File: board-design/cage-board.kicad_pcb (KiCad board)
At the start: 2 copper layers, 127 x 127 mm, 48 parts, among them J1 Jack-DC, J10 73131-0240, J11 73131-0240, J12 73131-0240, J13 Conn_01x02, J14 Conn_01x02, J2 Conn_02x17_Ribbon, J3 TB002-500-03BE, J4 73131-0240, J5 73131-0240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

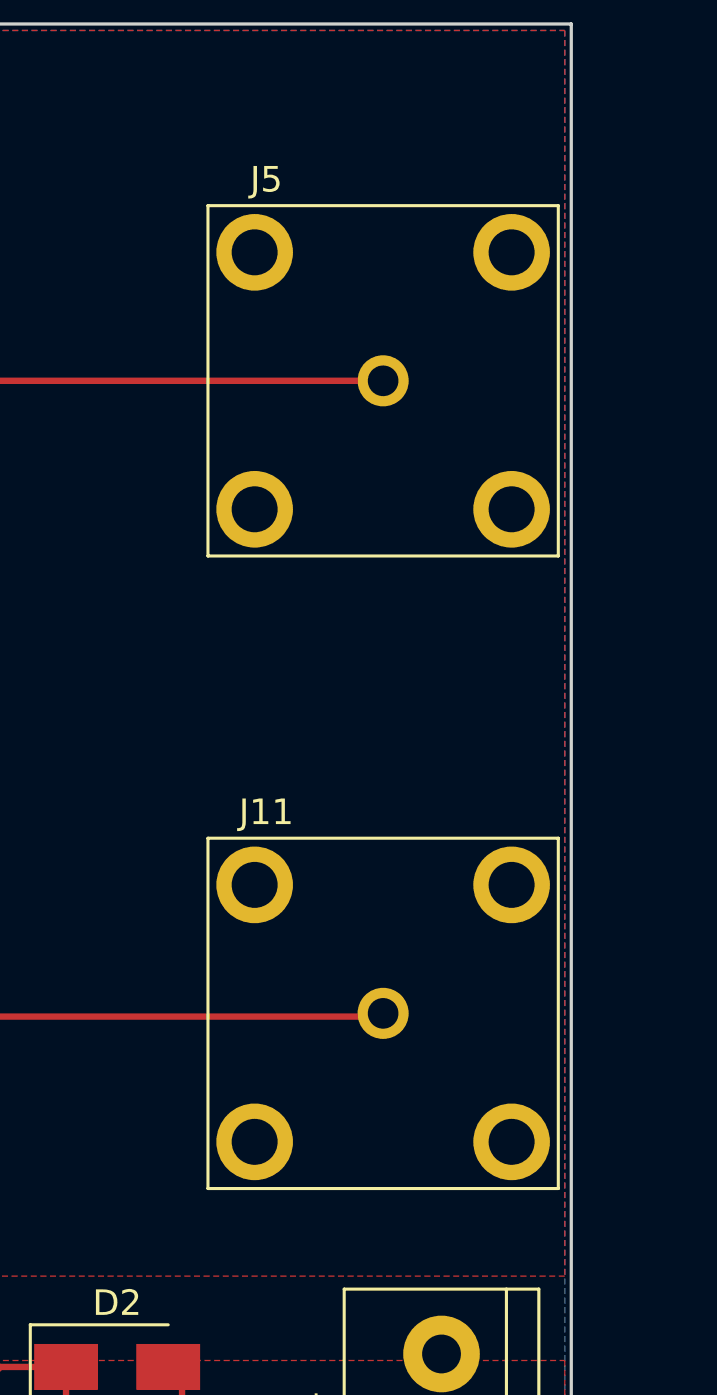
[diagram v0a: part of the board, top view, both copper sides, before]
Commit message: Add some 3D models
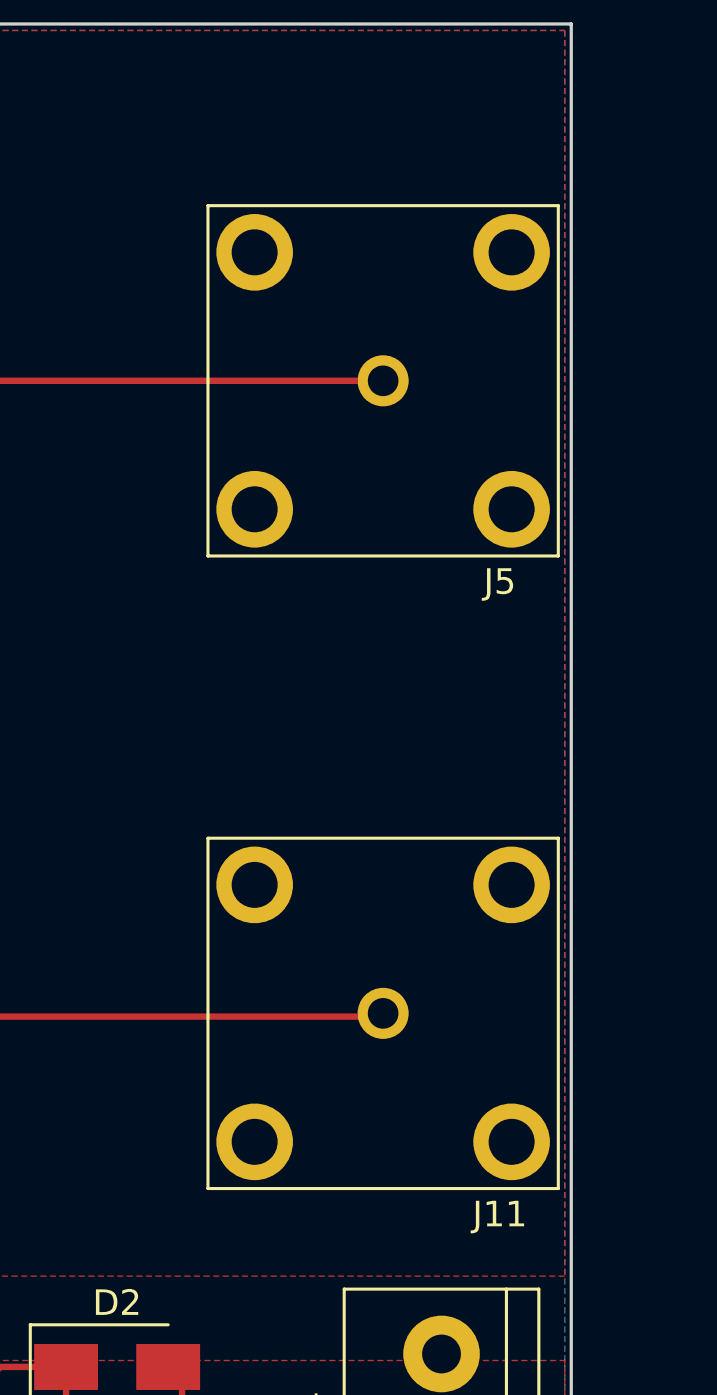
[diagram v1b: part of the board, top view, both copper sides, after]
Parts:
- J10, J11, J12, J4, J5, J6, J8: footprint chen-lab:BNC-Chen -> chen-lab:BNC-Chen-3D
- J3, J7, J9: footprint TerminalBlock:TerminalBlock_bornier-3_P5.08mm -> chen-lab:TerminalBlock_bornier-3_P5.08mm-3D
- turned J11 to 180 degrees
- turned J5 to 180 degrees

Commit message: more 3D models
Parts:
- J13, J14: footprint TerminalBlock:TerminalBlock_bornier-2_P5.08mm -> chen-lab:TerminalBlock_bornier-2_P5.08mm-3D

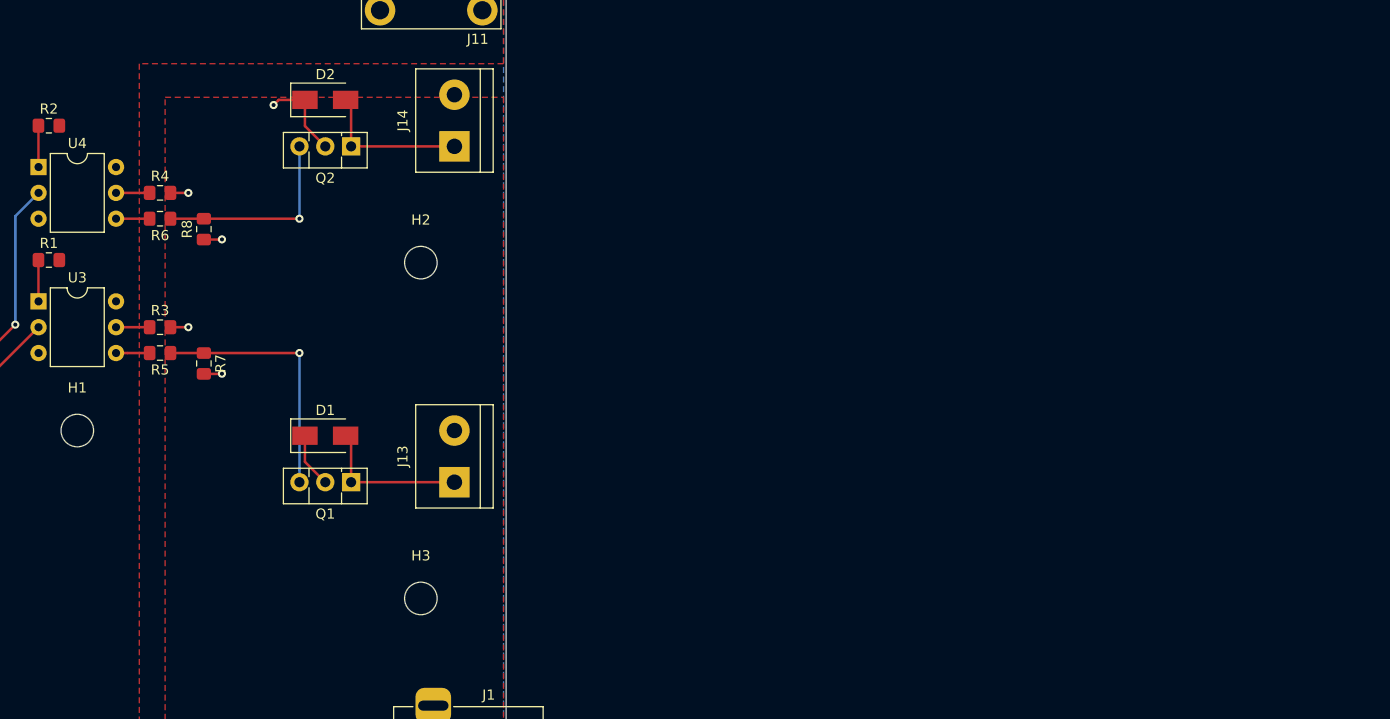
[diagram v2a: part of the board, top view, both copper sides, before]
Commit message: Add USB board with 3D
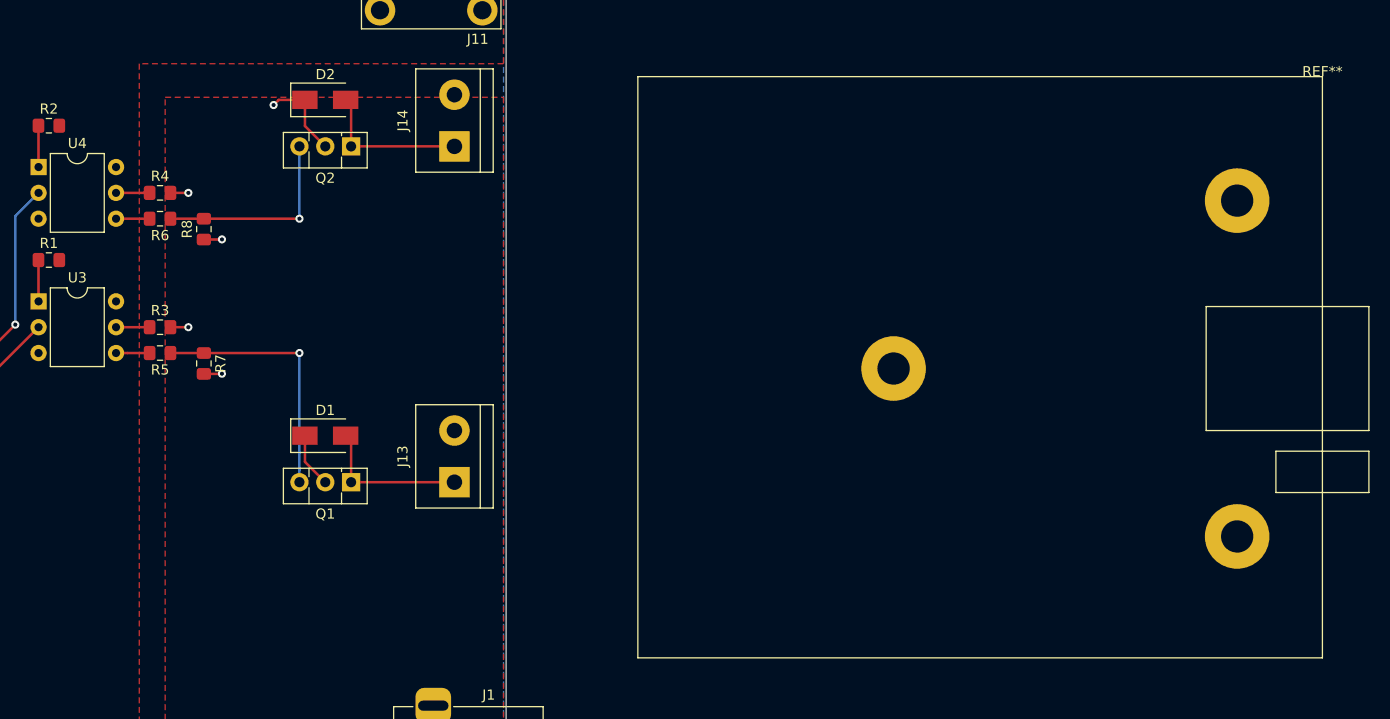
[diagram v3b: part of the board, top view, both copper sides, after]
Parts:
- removed H1, H2, H3: MountingHole, MountingHole:MountingHole_3.2mm_M3
- added REF**: usb-6501-oem, chen-lab:usb-6501-oem, F.Cu at (283.5, 75.7)

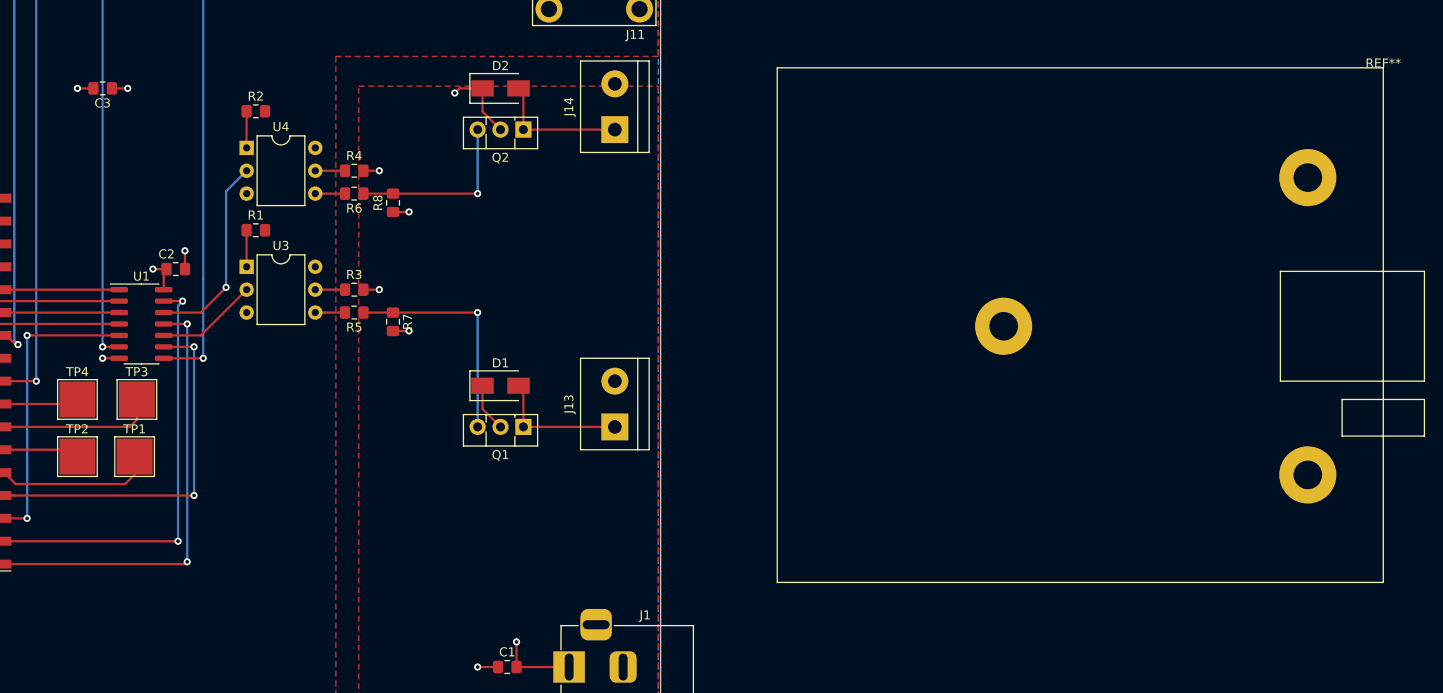
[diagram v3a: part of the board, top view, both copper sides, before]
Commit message: Raise USB board to 0.75in height
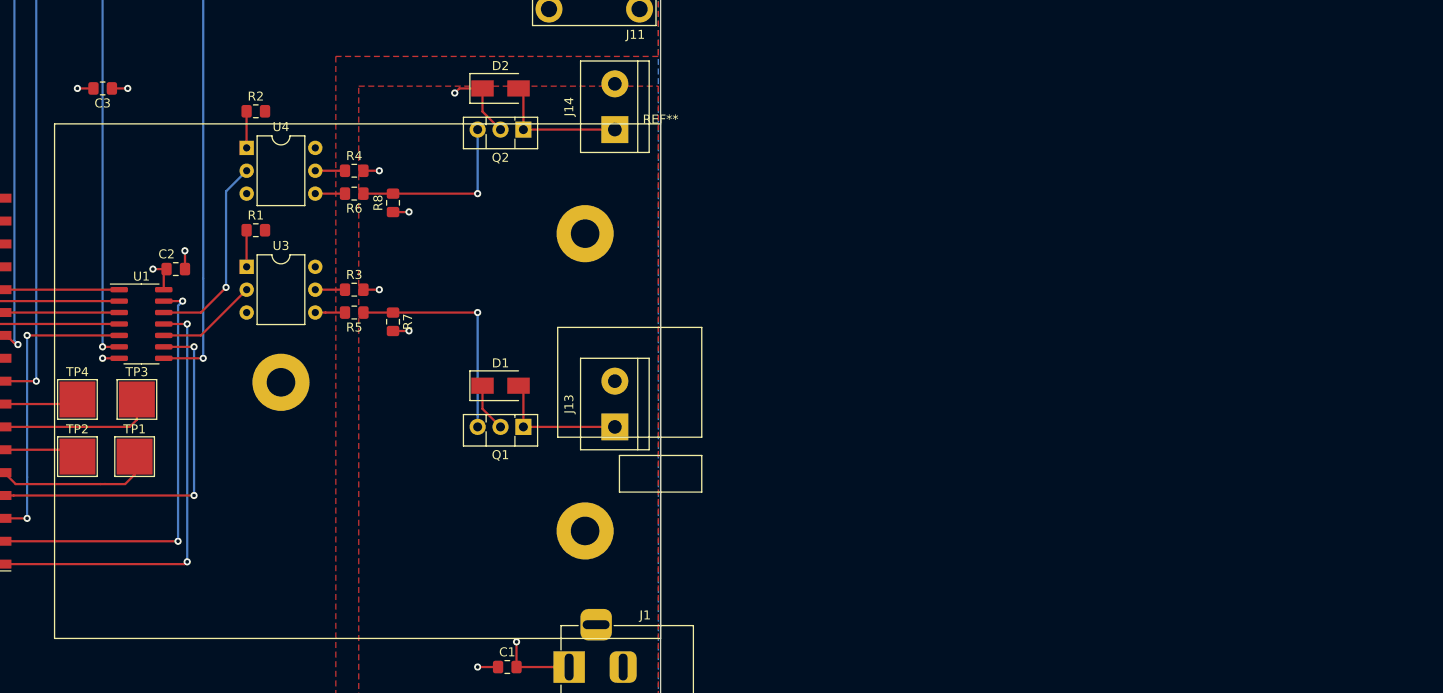
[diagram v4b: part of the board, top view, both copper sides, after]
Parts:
- moved REF** 80.5 mm to (203.2, 81.9)

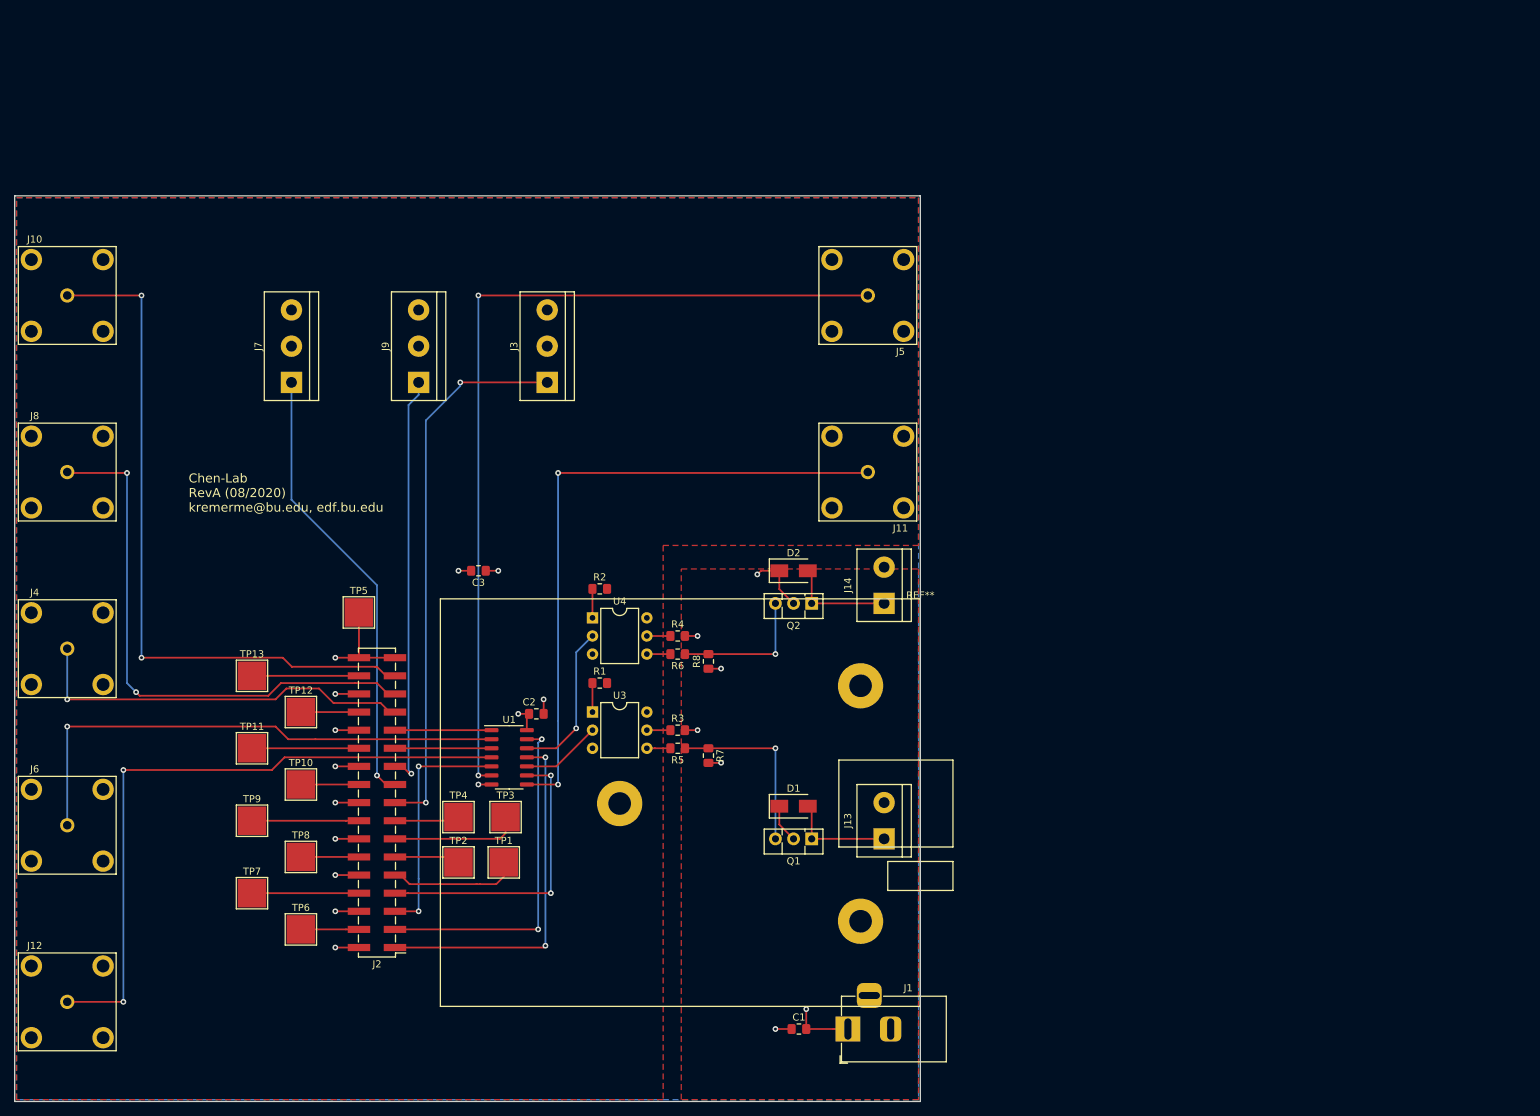
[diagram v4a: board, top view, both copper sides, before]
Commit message: moved screw terminals and updated test points
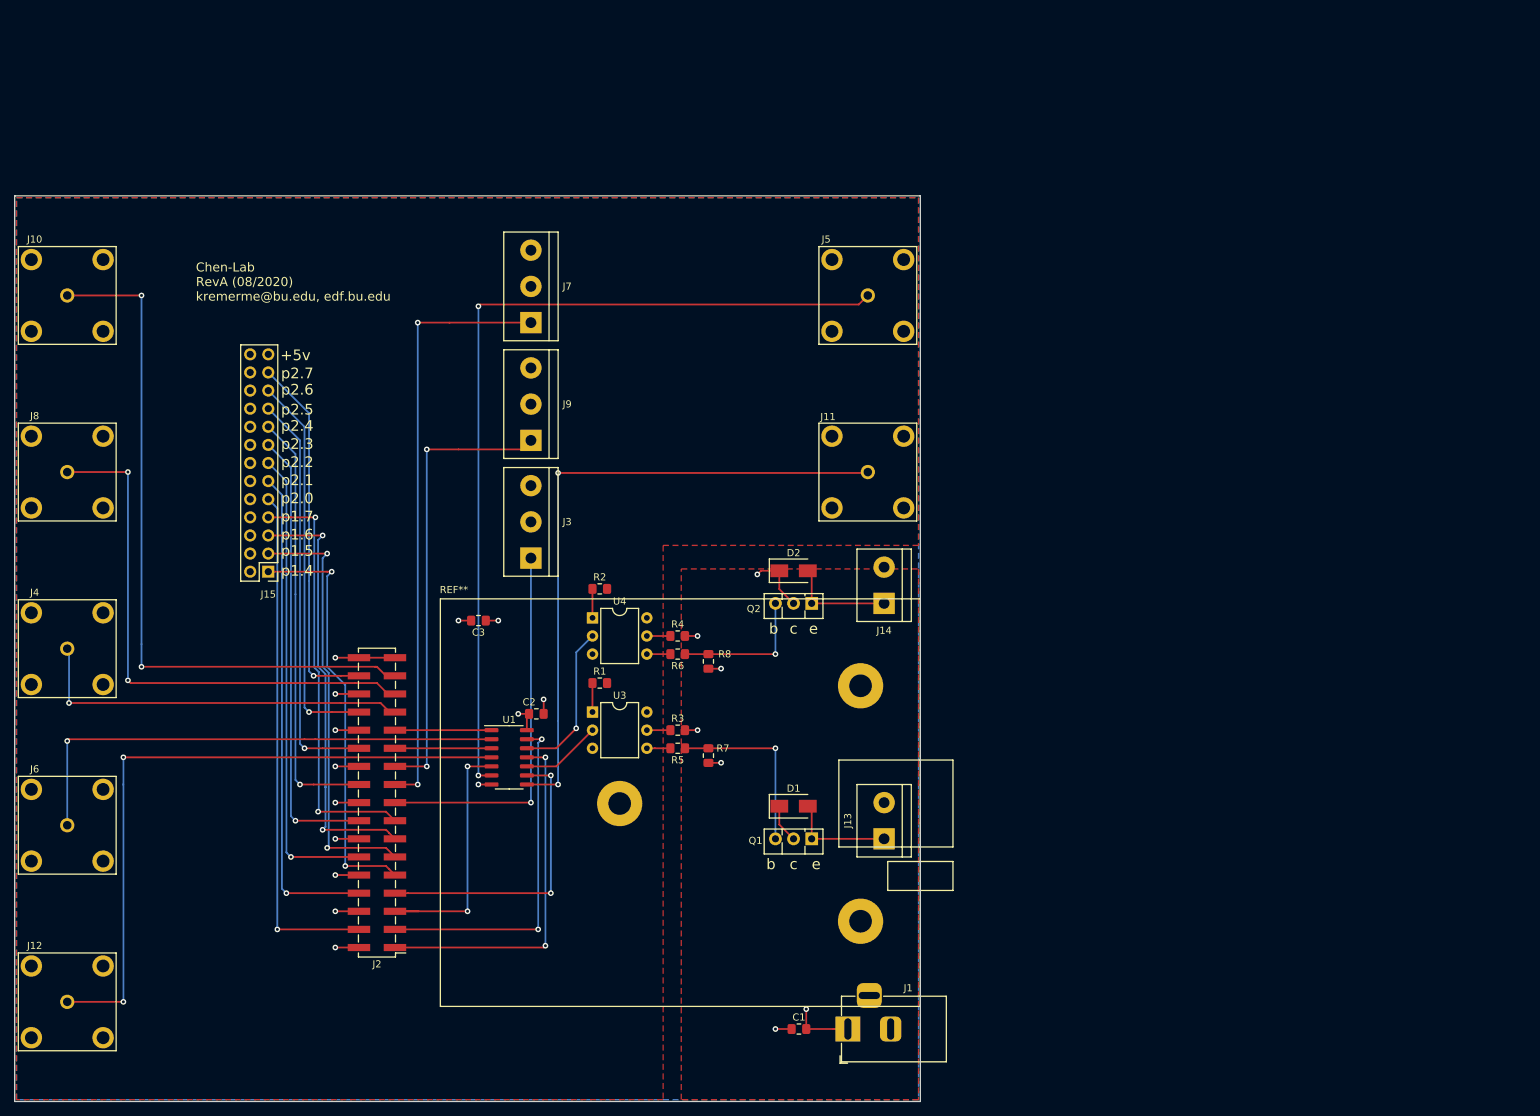
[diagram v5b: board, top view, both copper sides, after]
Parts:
- removed TP1, TP10, TP11, TP12, TP13, TP2, TP3, TP4, TP5, TP6, TP7, TP8, TP9: Pad, TestPoint:TestPoint_Pad_4.0x4.0mm
- added J15: Conn_02x13_test_points, Connector_PinHeader_2.54mm:PinHeader_2x13_P2.54mm_Vertical, F.Cu at (111.8, 78.1)
- J10, J11, J12, J4, J5, J6, J8: footprint chen-lab:BNC-Chen-3D -> chen-lab:BNC-Chen
- J13, J14: footprint chen-lab:TerminalBlock_bornier-2_P5.08mm-3D -> TerminalBlock:TerminalBlock_bornier-2_P5.08mm
- J3, J7, J9: footprint chen-lab:TerminalBlock_bornier-3_P5.08mm-3D -> TerminalBlock:TerminalBlock_bornier-3_P5.08mm
- moved J7 34.6 mm to (148.6, 43.2)
- moved J3 24.7 mm to (148.6, 76.2)
- moved J9 17.7 mm to (148.6, 59.7)
- moved C3 6.98 mm to (141.2, 85.0)
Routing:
- net /P2.0: track 8.14 -> 72.3 mm, vias 0 -> 1
- net /P2.2: track 8.14 -> 66.1 mm, vias 0 -> 1
- net /P2.1: track 15.0 -> 69.0 mm, vias 0 -> 1
- net /P2.4: track 8.14 -> 60.3 mm, vias 0 -> 1
- net /P1.5: track 9.12 -> 60.3 mm, vias 0 -> 2
- net /P1.7: track 9.12 -> 59.3 mm, vias 0 -> 2
- net /P2.3: track 15.0 -> 63.2 mm, vias 0 -> 1
- net /P2.6: track 8.14 -> 54.5 mm, vias 0 -> 1
- net /P1.6: track 18.1 -> 60.6 mm, vias 0 -> 2
- net /P2.5: track 15.0 -> 57.4 mm, vias 0 -> 1
- net /P1.4: track 18.5 -> 59.0 mm, vias 0 -> 2
- net /P2.7: track 15.0 -> 51.5 mm, vias 0 -> 1
- net /P0.0: track 77.5 -> 53.4 mm, vias 2 -> 1
- net /P0.1: track 63.1 -> 83.8 mm, vias 1 -> 2
- net +5V: track 20.4 -> 14.1 mm
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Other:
- board text added: "+5v"
- board text added: "b"
- board text added: "c"
- board text added: "e"
- board text added: "p1.4"
- board text added: "p1.5"
- board text added: "p1.6"
- board text added: "p1.7"
- board text added: "p2.0"
- board text added: "p2.1"
- board text added: "p2.2"
- board text added: "p2.3"
- board text added: "p2.4"
- board text added: "p2.5"
- board text added: "p2.6"
- board text added: "p2.7"
- board text removed: "Will NPN bump into Mez card?"
- board text removed: "make sure to check clearances for connectors"
